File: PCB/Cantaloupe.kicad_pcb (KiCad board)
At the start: 2 copper layers, 149.9 x 122.2 mm, 131 parts, among them J1 OLED, J2 Trackpad, J3 USB_In, J4 Split_comm_link, J5 RGB_Out, J6 SWD, J7 Extra, Q1 AO6802, SW1 MX, SW10 MX, SW11 MX, SW12 MX, SW13 MX, SW14 MX, SW15 MX, SW16 MX, SW17 MX, SW18 MX, SW19 MX, SW2 MX, SW20 MX, SW21 MX, SW22 MX, SW23 MX, SW24 MX, SW25 MX, SW26 MX, SW27 MX, SW28 MX, SW29 MX, SW3 MX, SW30 MX, SW31 Encoder, SW32 Reset, SW4 MX, SW5 MX, SW6 MX, SW7 MX, SW8 MX, SW9 MX, U1 STM32F401CCU6, U2 XC6206P332MR, U3 SRV05-4, U4 SRV05-4, U5 MB85RS64, U6 W25Q128JVS, Y1 8MHz

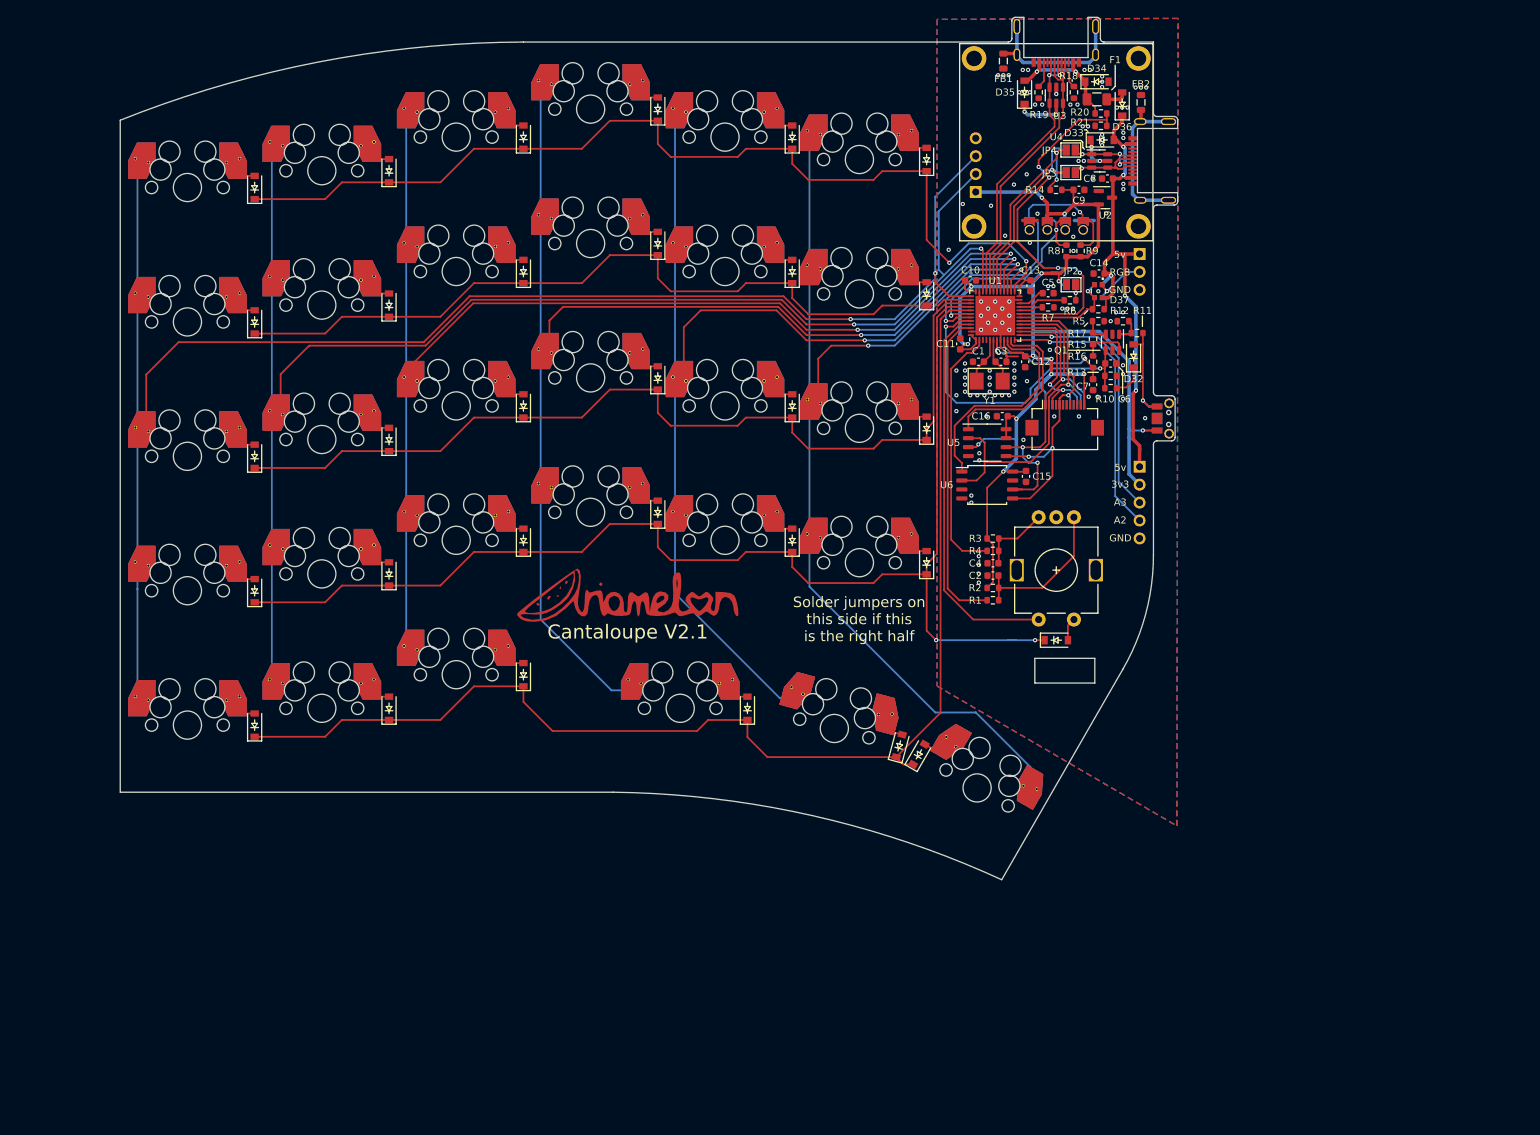
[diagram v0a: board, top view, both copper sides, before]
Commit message: Further updates to V2.1
Fixed mistakes with bottom cases. Added piece which is meant to mate with the button, allowing the reset to be pressed without needing a screwdriver. Update to USB port name and footprint (no functional change). Updated pin assignments. Rerouted board.
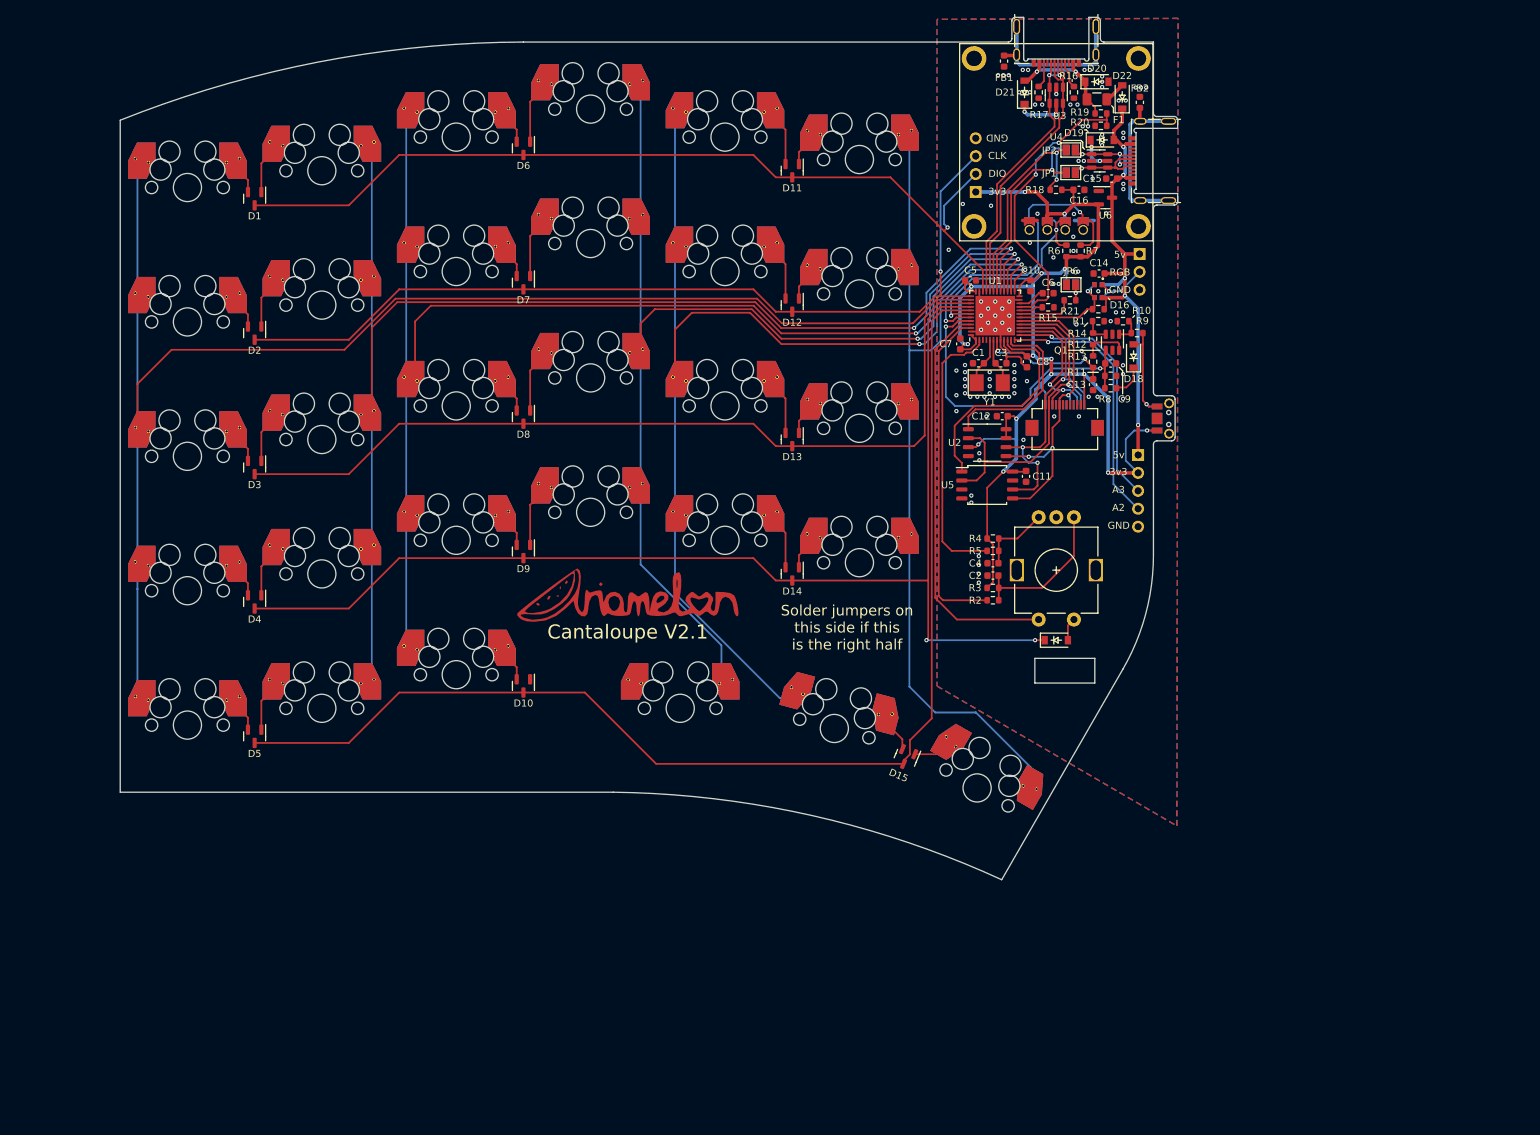
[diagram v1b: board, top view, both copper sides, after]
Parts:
- removed the D16 at (90.6, 27.5)
- removed the D17 at (90.6, 46.6)
- removed the D18 at (90.6, 65.6)
- removed the D19 at (90.6, 84.7)
- removed the D20 at (103.3, 112.4)
- removed the D21 at (109.6, 31.5)
- removed the D22 at (109.6, 50.5)
- removed D23, D24, D25, D26, D27, D28, D29, D30: D, Ariamelon:D_SOD-123
- removed the J7 at (158.8, 78.2)
- added J5: Extra, Ariamelon:PinHeader_1x05_P2.54mm_Vertical_Silkless, F.Cu at (158.6, 76.5)
- D1, D10, D11, D12, D13, D14, D15, D2, D3, D4, D5, D6, D7, D8, D9: value D -> D_Dual_CommonCathode_AAK_Split_Small; footprint Ariamelon:D_SOD-123 -> Package_TO_SOT_SMD:SOT-23
- FB1, FB2: footprint Inductor_SMD:L_0805_2012Metric -> Inductor_SMD:L_0603_1608Metric
- J6: renamed from J3; footprint Ariamelon:USB-C-C168688 -> Ariamelon:HRO-TYPE-C-31-M-13x
- J7: renamed from J4; footprint Ariamelon:USB-C-C168688 -> Ariamelon:HRO-TYPE-C-31-M-13x
- moved D15 55.5 mm to (125.7, 119.5), turned to -112.5 degrees
- moved D11 38.4 mm to (109.6, 36.2), turned to -90 degrees
- moved D13 38.4 mm to (109.6, 74.3), turned to -90 degrees
- moved D14 38.4 mm to (109.6, 93.4), turned to -90 degrees
- moved D12 38.4 mm to (109.6, 55.3), turned to -90 degrees
- moved D10 19.3 mm to (71.5, 109.3), turned to -90 degrees
- moved D6 19.3 mm to (71.5, 33.1), turned to -90 degrees
- moved D7 19.3 mm to (71.5, 52.1), turned to -90 degrees
- moved D8 19.3 mm to (71.5, 71.2), turned to -90 degrees
- moved D9 19.3 mm to (71.5, 90.2), turned to -90 degrees
- moved D2 1.59 mm to (33.4, 59.3), turned to -90 degrees
- moved D1 1.59 mm to (33.4, 40.2), turned to -90 degrees
- moved D3 1.59 mm to (33.4, 78.3), turned to -90 degrees
- moved D4 1.59 mm to (33.4, 97.4), turned to -90 degrees
- moved D5 1.59 mm to (33.4, 116.4), turned to -90 degrees
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- renumbered C13 to C10, C15 to C11, C16 to C12, C7 to C13, C8 to C15, C9 to C16, C10 to C5, C5 to C6, C11 to C7, C12 to C8, C6 to C9, D37 to D16, D31 to D17, D32 to D18, D33 to D19, D34 to D20, D35 to D21, D36 to D22, J5 to J1, J6 to J2, J2 to J3, J1 to J4, JP3 to JP1, JP4 to JP2, JP5 to JP3, JP6 to JP4, JP1 to JP5, JP2 to JP6, R5 to R1, R12 to R10, R13 to R11, R15 to R12, R16 to R13, R17 to R14, R7 to R15, R18 to R16, R19 to R17, R14 to R18, R20 to R19, R1 to R2, R21 to R20, R6 to R21, R2 to R3, R3 to R4, R4 to R5, R8 to R6, R9 to R7, R10 to R8, R11 to R9, U5 to U2, U6 to U5, U2 to U6
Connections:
- D1 pad 1: ROW0 -> Net-(D1-Pad1)
- D10 pad 1: ROW4 -> Net-(D10-Pad1)
- D11 pad 1: ROW0 -> Net-(D11-Pad1)
- D12 pad 1: ROW1 -> Net-(D12-Pad1)
- D13 pad 1: ROW2 -> Net-(D13-Pad1)
- D14 pad 1: ROW3 -> Net-(D14-Pad1)
- D15 pad 1: ROW4 -> Net-(D15-Pad1)
- D2 pad 1: ROW1 -> Net-(D2-Pad1)
- D3 pad 1: ROW2 -> Net-(D3-Pad1)
- D4 pad 1: ROW3 -> Net-(D4-Pad1)
- D5 pad 1: ROW4 -> Net-(D5-Pad1)
- D6 pad 1: ROW0 -> Net-(D6-Pad1)
- D7 pad 1: ROW1 -> Net-(D7-Pad1)
- D8 pad 1: ROW2 -> Net-(D8-Pad1)
- D9 pad 1: ROW3 -> Net-(D9-Pad1)
- J2 pad 2: COL1 -> ROW0
- J2 pad 3: COL0 -> ROW1
- SW10 pad 1: COL1 -> Net-(D5-Pad1)
- SW10 pad 2: Net-(D10-Pad2) -> COL1
- SW11 pad 2: Net-(D11-Pad2) -> Net-(D6-Pad2)
- SW12 pad 2: Net-(D12-Pad2) -> Net-(D7-Pad2)
- SW13 pad 2: Net-(D13-Pad2) -> Net-(D8-Pad2)
- SW14 pad 2: Net-(D14-Pad2) -> Net-(D9-Pad2)
- SW15 pad 2: Net-(D15-Pad2) -> Net-(D10-Pad2)
- SW16 pad 1: COL3 -> Net-(D6-Pad1)
- SW16 pad 2: Net-(D16-Pad2) -> COL3
- SW17 pad 1: COL3 -> Net-(D7-Pad1)
- SW17 pad 2: Net-(D17-Pad2) (its old number) -> COL3
- SW18 pad 1: COL3 -> Net-(D8-Pad1)
- SW18 pad 2: Net-(D18-Pad2) (its old number) -> COL3
- SW19 pad 1: COL3 -> Net-(D9-Pad1)
- SW19 pad 2: Net-(D19-Pad2) -> COL3
- SW20 pad 1: COL3 -> Net-(D10-Pad1)
- SW20 pad 2: Net-(D20-Pad2) -> COL3
- SW21 pad 2: Net-(D21-Pad2) -> Net-(D11-Pad2)
- SW22 pad 2: Net-(D22-Pad2) (its old number) -> Net-(D12-Pad2)
- SW23 pad 2: Net-(D23-Pad2) -> Net-(D13-Pad2)
- SW24 pad 2: Net-(D24-Pad2) -> Net-(D14-Pad2)
- SW25 pad 2: Net-(D25-Pad2) -> Net-(D15-Pad2)
- SW26 pad 1: COL5 -> Net-(D11-Pad1)
- SW26 pad 2: Net-(D26-Pad2) -> COL5
- SW27 pad 1: COL5 -> Net-(D12-Pad1)
- SW27 pad 2: Net-(D27-Pad2) -> COL5
- SW28 pad 1: COL5 -> Net-(D13-Pad1)
- SW28 pad 2: Net-(D28-Pad2) -> COL5
- SW29 pad 1: COL5 -> Net-(D14-Pad1)
- SW29 pad 2: Net-(D29-Pad2) -> COL5
- SW30 pad 1: Net-(D30-Pad2) -> Net-(D15-Pad1)
- SW6 pad 1: COL1 -> Net-(D1-Pad1)
- SW6 pad 2: Net-(D6-Pad2) -> COL1
- SW7 pad 1: COL1 -> Net-(D2-Pad1)
- SW7 pad 2: Net-(D7-Pad2) -> COL1
- SW8 pad 1: COL1 -> Net-(D3-Pad1)
- SW8 pad 2: Net-(D8-Pad2) -> COL1
- SW9 pad 1: COL1 -> Net-(D4-Pad1)
- SW9 pad 2: Net-(D9-Pad2) -> COL1
- U1 pad 19: PLUGGED -> Side
- U1 pad 21: Side -> PLUGGED
- U1 pad 25: ROW0 -> COL5
- U1 pad 26: COL5 -> COL4
- U1 pad 27: COL4 -> COL3
- U1 pad 28: COL3 -> COL2
- U1 pad 29: COL2 -> COL1
- U1 pad 34: COL1 -> ROW0
- U1 pad 37: COL0 -> ROW1
- U1 pad 38: ROW1 -> COL0
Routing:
- net COL5: track 149.0 -> 128.9 mm, vias 2 -> 1
- net COL0: track 229.8 -> 209.9 mm, vias 2 -> 0
- net PLUGGED: track 58.4 -> 41.5 mm, vias 4 -> 2
- net COL1: track 212.9 -> 196.4 mm
- net ROW1: track 114.6 -> 128.6 mm, vias 0 -> 1
- net ROW0: track 140.4 -> 126.3 mm, vias 2 -> 1
- net COL3: track 172.8 -> 160.7 mm
- net +3V3: track 207.3 -> 196.8 mm, vias 14 -> 15
- net ROW2: track 132.0 -> 124.0 mm
- net ROW3: track 176.9 -> 168.9 mm
- net Net-(D9-Pad1): track 0.00 -> 7.78 mm
- net Net-(D8-Pad1): track 0.00 -> 7.78 mm
- net Net-(D7-Pad1): track 0.00 -> 7.78 mm
- net Net-(D6-Pad1): track 0.00 -> 7.78 mm
- net COL4: track 154.9 -> 161.9 mm
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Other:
- outline, holes or cut-outs redrawn
- board text added: "CLK"
- board text added: "DIO"

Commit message: Added another 10u filtering cap. Rerouted power track. Changed pin assignments. Changed values of VBUS detect to use already existing values on the board.
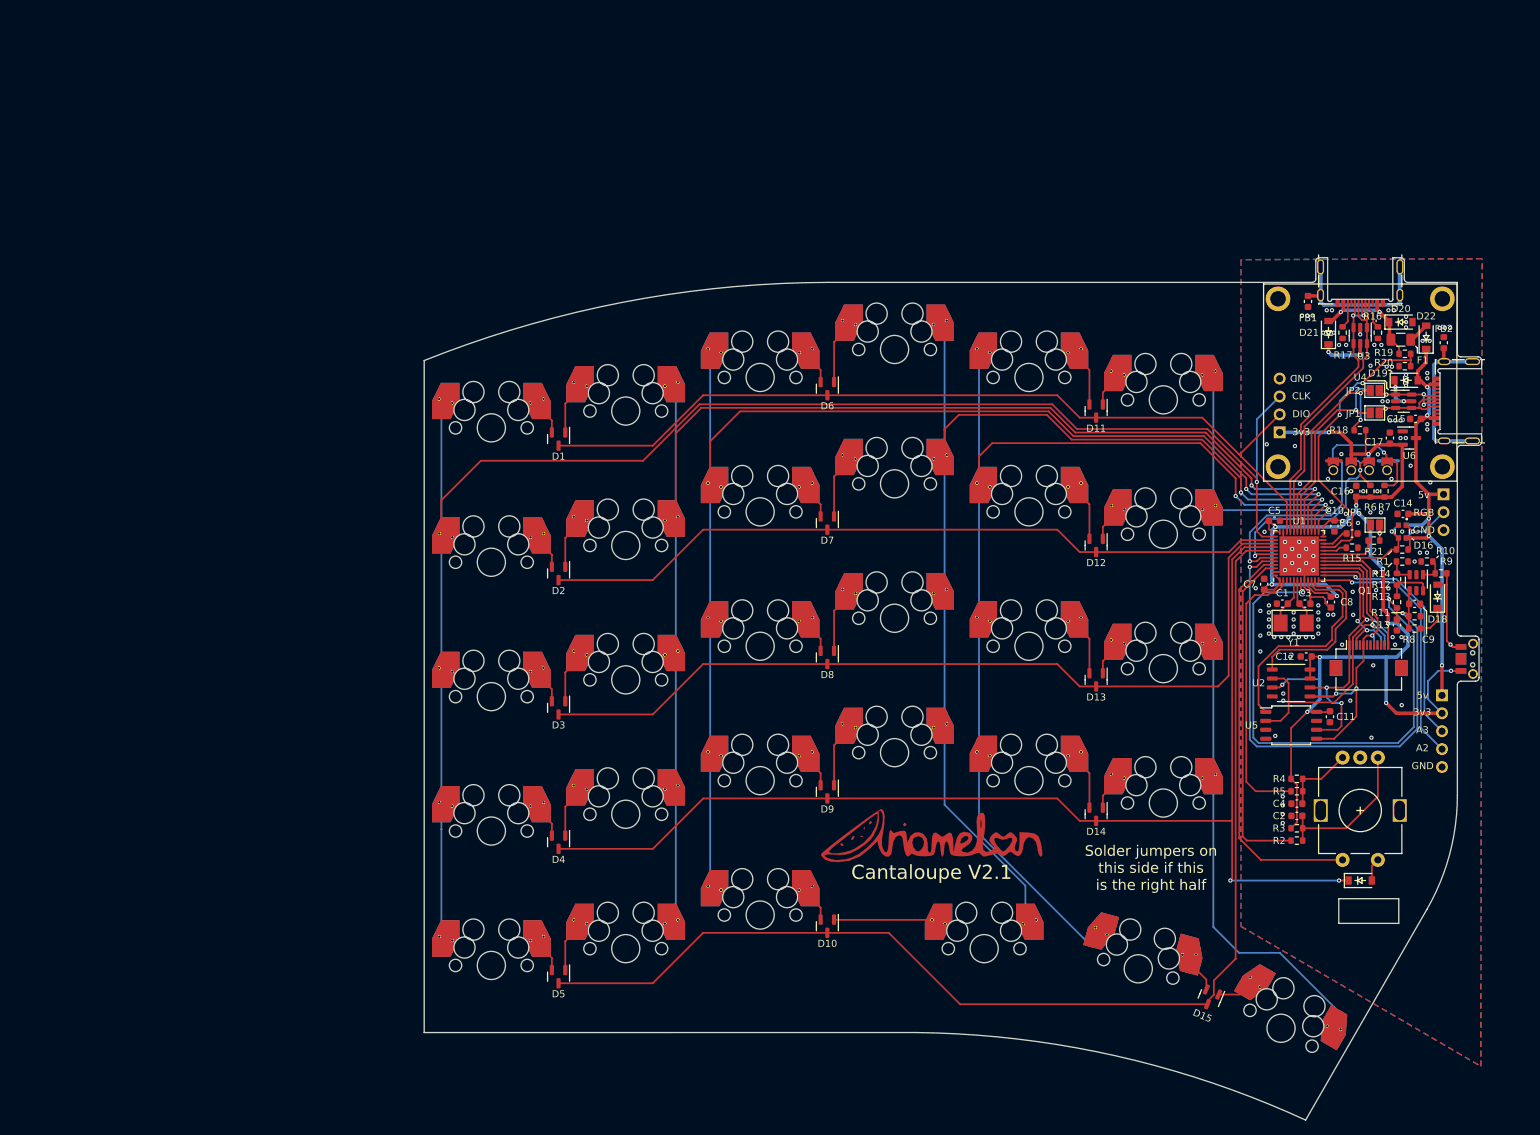
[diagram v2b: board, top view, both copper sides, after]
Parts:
- added C17: 10u, Capacitor_SMD:C_0603_1608Metric, F.Cu at (194.3, 74.1)
- moved C16 58.1 mm to (189.6, 81.7), turned to -90 degrees
- moved SW1 54.9 mm to (67.0, 72.7)
- moved SW10 54.9 mm to (86.0, 146.5)
- moved SW14 54.9 mm to (105.1, 122.7)
- moved SW3 54.9 mm to (67.0, 110.8)
- moved SW6 54.9 mm to (86.0, 70.3)
- moved SW9 54.9 mm to (86.0, 127.5)
- moved C1 54.9 mm to (179.1, 97.6)
- moved C14 54.9 mm to (196.2, 84.9)
- moved C2 54.9 mm to (181.1, 127.7)
- moved C4 54.9 mm to (181.1, 126.0)
- moved C7 54.9 mm to (176.5, 94.9)
- moved C9 54.9 mm to (197.8, 97.6)
- moved D1 54.9 mm to (76.5, 74.3)
- moved D10 54.9 mm to (114.6, 143.3)
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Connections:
- J2 pad 3: ROW1 -> COL0
- U1 pad 37: ROW1 -> COL0
- U1 pad 38: COL0 -> ROW1
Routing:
- net NRST: track 18.3 -> 75.5 mm
- net BOOT0: track 45.1 -> 77.1 mm
- net ROW1: track 128.6 -> 106.5 mm, vias 1 -> 0
- net COL0: track 209.9 -> 231.8 mm, vias 0 -> 1
- net Net-(D10-Pad1): track 0.00 -> 13.9 mm
- net COL5: track 128.9 -> 119.9 mm
- net COL4: track 161.9 -> 154.5 mm
- net +3V3: track 196.8 -> 200.7 mm, vias 15 -> 14
- net MOSI: track 45.7 -> 48.8 mm
- net COL3: track 160.7 -> 158.0 mm
- net COL1: track 196.4 -> 193.7 mm
- net SS_TP: track 22.1 -> 20.4 mm
- net ROW0: track 126.3 -> 124.8 mm, vias 1 -> 0
- net SCL: track 34.0 -> 34.7 mm
- net SDA: track 46.4 -> 47.0 mm
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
